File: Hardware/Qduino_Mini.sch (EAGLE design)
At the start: 43 parts, among them Q1 PFET, U1 ATMEGA32U41:1-LESS_PASTE, U2 MCP73831, U3 MAX17048, U4 TPS78233, U5 MIGHTYQ-L-SILK, U6 MIGHTYQ-S-SILK, U7 DNP, Y1 8MHZ

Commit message: Added info on safe voltages & oscillator speeds
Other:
- note added: "ATmega32U4 VCC = 3.3V & F_OSC = 8MHz"
- note added: "Set for 100mA charging"
- note added: "USB BUS (USB spec voltages)"
- note removed: "ATmega32U4 3.3V @ 16MHz"
- note removed: "Can only run up to 13.3MHz @ 3V"
- note removed: "Set for 500mA charging"
- note removed: "USB BUS"
- moved on the sheet: JP2, R6, R7
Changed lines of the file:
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@@
 <sheet>
 <plain>
-<text x="38.1" y="119.38" size="1.778" layer="97" align="center">Set for 500mA charging</text>
-<text x="0" y="15.24" size="2.54" layer="97" align="center">USB BUS</text>
+<text x="38.1" y="119.38" size="1.778" layer="97" align="center">Set for 100mA charging</text>
+<text x="12.7" y="15.24" size="2.54" layer="97" align="center">USB BUS
+(USB spec voltages)</text>
 <text x="60.96" y="15.24" size="2.54" layer="97" align="center">Resonator</text>
 <text x="53.34" y="73.66" size="2.54" layer="97" align="center">Status LEDs</text>
@@
 <text x="129.54" y="66.04" size="1.778" layer="97">SPST</text>
 <text x="-55.88" y="124.46" size="2.54" layer="97" align="center">ATmega32U4
-3.3V @ 16MHz</text>
+VCC = 3.3V &amp; F_OSC = 8MHz</text>
 <wire x1="-20.32" y1="134.62" x2="-20.32" y2="78.74" width="0.4064" layer="97" style="shortdash"/>
 <wire x1="-20.32" y1="78.74" x2="-20.32" y2="27.94" width="0.4064" layer="97" style="shortdash"/>
@@
 <text x="-2.54" y="73.66" size="2.54" layer="97" align="center">I2C PULLUPS</text>
 <wire x1="12.7" y1="78.74" x2="12.7" y2="20.32" width="0.4064" layer="97" style="shortdash"/>
-<text x="41.91" y="-13.97" size="1.6764" layer="97">Can only run up to 13.3MHz @ 3V</text>
 <text x="62.23" y="-43.18" size="2.54" layer="94" ratio="5">Revised by: Brent Wilkins</text>
 </plain>
@@
 </instance>
 <instance part="R8" gate="G$1" x="63.5" y="93.98" rot="R90"/>
-<instance part="R6" gate="G$1" x="25.4" y="-2.54" rot="R180">
+<instance part="R6" gate="G$1" x="25.4" y="5.08" rot="R180">
+<attribute name="PROD_ID" x="25.4" y="5.08" size="1.27" layer="96" rot="R180" display="off"/>
+</instance>
+<instance part="R7" gate="G$1" x="25.4" y="-2.54" rot="R180">
 <attribute name="PROD_ID" x="25.4" y="-2.54" size="1.27" layer="96" rot="R180" display="off"/>
-</instance>
-<instance part="R7" gate="G$1" x="25.4" y="5.08" rot="R180">
-<attribute name="PROD_ID" x="25.4" y="5.08" size="1.27" layer="96" rot="R180" display="off"/>
 </instance>
 <instance part="R2" gate="G$1" x="38.1" y="38.1" rot="R270">
@@
 <instance part="FID5" gate="G$1" x="157.48" y="-25.4"/>
 <instance part="FID6" gate="G$1" x="157.48" y="-17.78"/>
-<instance part="GND10" gate="1" x="12.7" y="5.08"/>
-<instance part="JP2" gate="G$1" x="-5.08" y="0" smashed="yes" rot="R180">
-<attribute name="NAME" x="-0.254" y="-8.128" size="1.778" layer="95" rot="R180"/>
+<instance part="GND10" gate="1" x="7.62" y="-10.16"/>
+<instance part="JP2" gate="G$1" x="-2.54" y="0" smashed="yes" rot="MR0">
+<attribute name="NAME" x="2.286" y="8.128" size="1.778" layer="95" rot="MR0"/>
 </instance>
 <instance part="GND11" gate="1" x="-15.24" y="-5.08"/>
@@
 <net name="D-" class="0">
 <segment>
-<wire x1="30.48" y1="-2.54" x2="33.02" y2="-2.54" width="0.1524" layer="91"/>
+<wire x1="30.48" y1="5.08" x2="33.02" y2="5.08" width="0.1524" layer="91"/>
 <pinref part="R6" gate="G$1" pin="1"/>
-<label x="33.02" y="-2.54" size="1.27" layer="95" xref="yes"/>
+<label x="33.02" y="5.08" size="1.27" layer="95" xref="yes"/>
 </segment>
 <segment>
@@
 <net name="D+" class="0">
 <segment>
-<wire x1="33.02" y1="5.08" x2="30.48" y2="5.08" width="0.1524" layer="91"/>
+<wire x1="33.02" y1="-2.54" x2="30.48" y2="-2.54" width="0.1524" layer="91"/>
 <pinref part="R7" gate="G$1" pin="1"/>
-<label x="33.02" y="5.08" size="1.27" layer="95" xref="yes"/>
+<label x="33.02" y="-2.54" size="1.27" layer="95" xref="yes"/>
 </segment>
 <segment>
@@
 <pinref part="GND11" gate="1" pin="GND"/>
 <wire x1="-15.24" y1="-2.54" x2="-15.24" y2="0" width="0.1524" layer="91"/>
-<wire x1="-15.24" y1="0" x2="-12.7" y2="0" width="0.1524" layer="91"/>
-</segment>
-<segment>
-<wire x1="7.62" y1="10.16" x2="12.7" y2="10.16" width="0.1524" layer="91"/>
+<wire x1="-15.24" y1="0" x2="-10.16" y2="0" width="0.1524" layer="91"/>
+</segment>
+<segment>
 <pinref part="GND10" gate="1" pin="GND"/>
-<wire x1="12.7" y1="7.62" x2="12.7" y2="10.16" width="0.1524" layer="91"/>
 <pinref part="JP2" gate="G$1" pin="GND"/>
-<wire x1="7.62" y1="10.16" x2="7.62" y2="5.08" width="0.1524" layer="91"/>
-<wire x1="7.62" y1="5.08" x2="2.54" y2="5.08" width="0.1524" layer="91"/>
+<wire x1="7.62" y1="-7.62" x2="7.62" y2="-5.08" width="0.1524" layer="91"/>
+<wire x1="7.62" y1="-5.08" x2="5.08" y2="-5.08" width="0.1524" layer="91"/>
 </segment>
 <segment>
@@
 <segment>
 <pinref part="R6" gate="G$1" pin="2"/>
-<wire x1="20.32" y1="-2.54" x2="2.54" y2="-2.54" width="0.1524" layer="91"/>
+<wire x1="20.32" y1="5.08" x2="17.78" y2="5.08" width="0.1524" layer="91"/>
+<wire x1="17.78" y1="5.08" x2="17.78" y2="2.54" width="0.1524" layer="91"/>
+<wire x1="17.78" y1="2.54" x2="5.08" y2="2.54" width="0.1524" layer="91"/>
 <pinref part="JP2" gate="G$1" pin="D-"/>
 </segment>
@@
 <pinref part="R7" gate="G$1" pin="2"/>
 <pinref part="JP2" gate="G$1" pin="D+"/>
-<wire x1="20.32" y1="5.08" x2="17.78" y2="5.08" width="0.1524" layer="91"/>
-<wire x1="17.78" y1="5.08" x2="17.78" y2="0" width="0.1524" layer="91"/>
-<wire x1="17.78" y1="0" x2="2.54" y2="0" width="0.1524" layer="91"/>
+<wire x1="20.32" y1="-2.54" x2="7.62" y2="-2.54" width="0.1524" layer="91"/>
+<wire x1="7.62" y1="-2.54" x2="7.62" y2="0" width="0.1524" layer="91"/>
+<wire x1="7.62" y1="0" x2="5.08" y2="0" width="0.1524" layer="91"/>
 </segment>
 </net>
@@
 <net name="VBUS" class="0">
 <segment>
-<label x="10.16" y="-5.08" size="1.27" layer="95" xref="yes"/>
+<label x="10.16" y="5.08" size="1.27" layer="95" xref="yes"/>
 <pinref part="JP2" gate="G$1" pin="VCC"/>
-<wire x1="10.16" y1="-5.08" x2="2.54" y2="-5.08" width="0.1524" layer="91"/>
-</segment>
-<segment>
+<wire x1="10.16" y1="5.08" x2="5.08" y2="5.08" width="0.1524" layer="91"/>
+</segment>
+<segment>

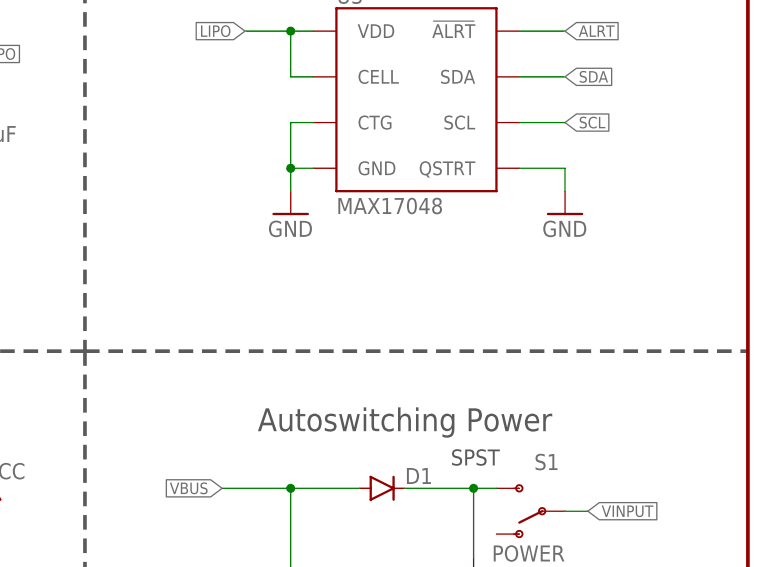
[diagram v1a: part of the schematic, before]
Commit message: Added I2C address to schematic for fuel gauge.  No change to PCB
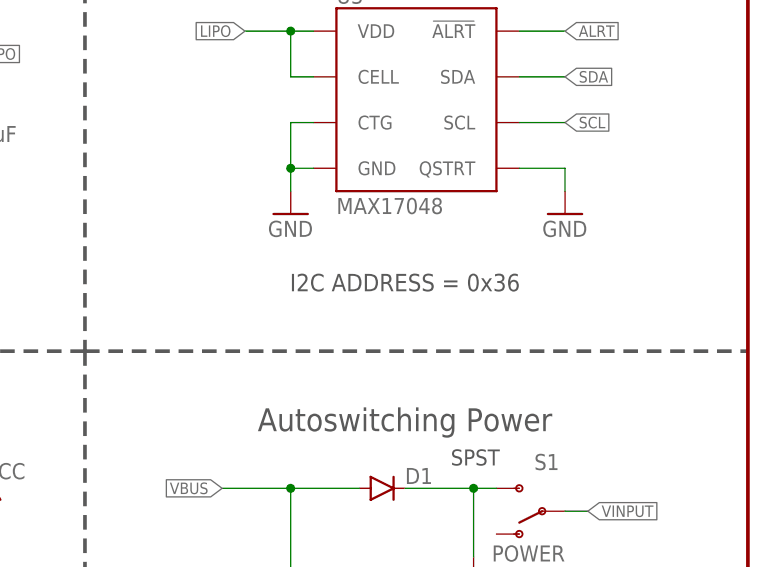
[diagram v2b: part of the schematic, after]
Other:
- note added: "I2C ADDRESS = 0x36"
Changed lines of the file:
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@@
 <wire x1="12.7" y1="78.74" x2="12.7" y2="20.32" width="0.4064" layer="97" style="shortdash"/>
 <text x="62.23" y="-43.18" size="2.54" layer="94" ratio="5">Revised by: Brent Wilkins</text>
+<text x="124.46" y="86.36" size="1.9304" layer="97" align="center">I2C ADDRESS = 0x36</text>
 </plain>
 <instances>

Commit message: Added 'IC-' prefix to the attriburtes of a part
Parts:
- U4: PROD_ID 12550 -> IC-12550
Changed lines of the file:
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@@
 <?xml version="1.0" encoding="utf-8"?>
 <!DOCTYPE eagle SYSTEM "eagle.dtd">
-<eagle version="7.2.0">
+<eagle version="7.3.0">
 <drawing>
 <settings>
@@
 <part name="GND15" library="SparkFun-Aesthetics" deviceset="GND" device=""/>
 <part name="U4" library="SparkFun-PowerIC" deviceset="LDO-TPS78233" device="" value="TPS78233">
-<attribute name="PROD_ID" value="12550"/>
+<attribute name="PROD_ID" value="IC-12550"/>
 </part>
 <part name="C9" library="SparkFun-Capacitors" deviceset="2.2UF-10V-20%(0603)" device="" value="2.2uF"/>
